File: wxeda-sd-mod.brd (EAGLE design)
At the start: 101.3 x 40.6 mm, 26 parts, among them T1 2N3904, U1 SD_CARD, X1 TV OUT, X2 TAPE IN / OUT

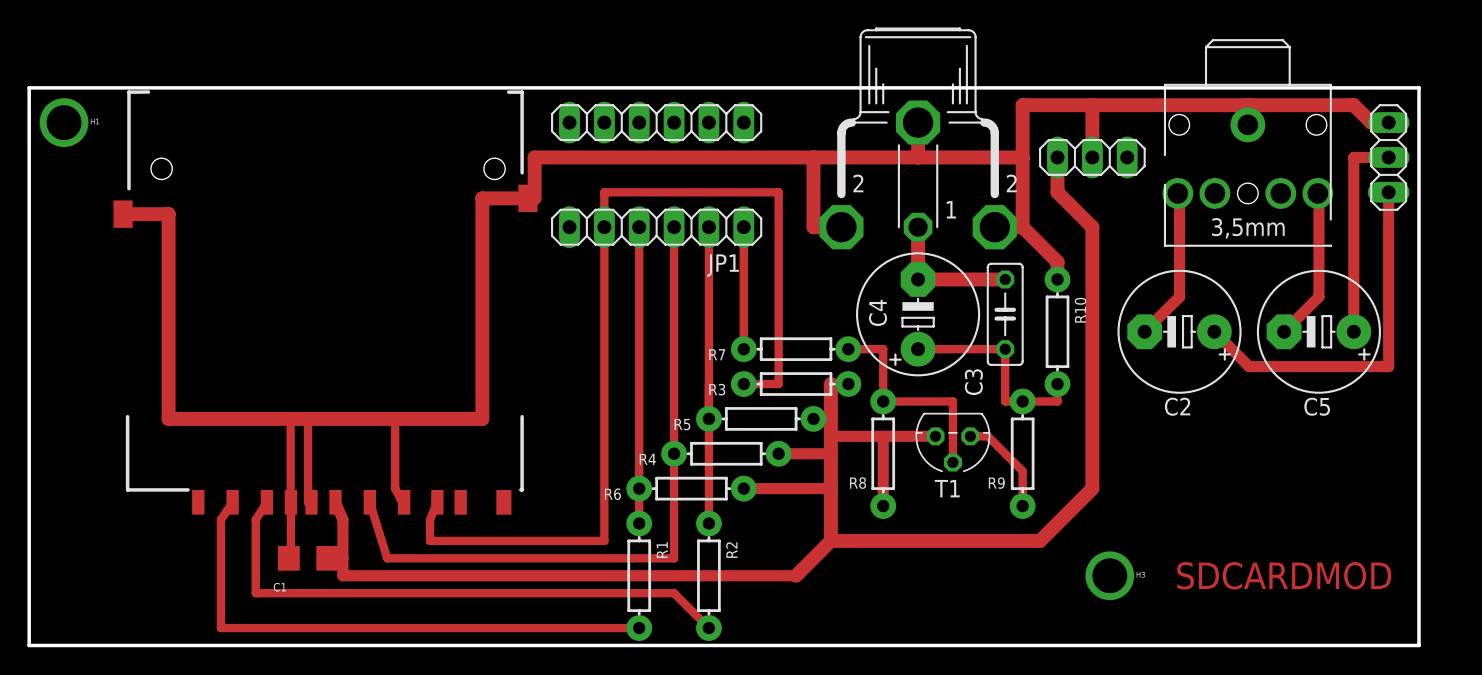
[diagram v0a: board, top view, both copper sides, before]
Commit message: Added stereo out
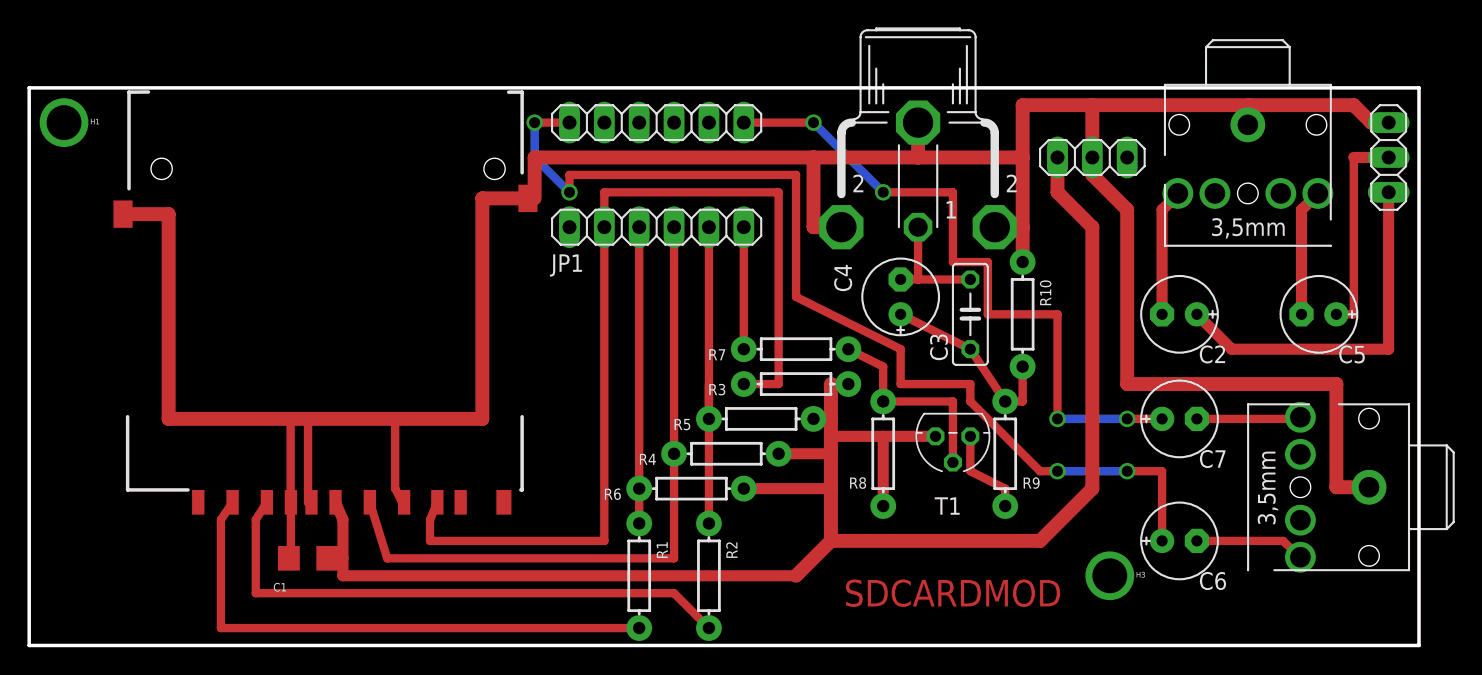
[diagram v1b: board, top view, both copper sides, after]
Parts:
- added C6, C7: 10uF, adafruit:E2,5-6E
- added X3: STEREO OUT, adafruit:STX3100
- C2, C4, C5: device adafruit:E5-8,5 -> adafruit:E2,5-6E
- moved R10 2.84 mm to (72.4, 24.1)
- moved C3 2.54 mm to (68.6, 24.1)
- moved C4 1.80 mm to (63.5, 25.4)
- moved C2 1.27 mm to (83.8, 24.1)
- moved C5 1.27 mm to (94.0, 24.1)
- moved R9 1.27 mm to (71.1, 14.0)
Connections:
- new net N$11: C7.-, X3.5
- new net N$9: C6.-, X3.2
- net DSB: now also C7.+
- net DSEN1: now also C6.+
- net GND: now also X3.1
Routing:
- net DSEN1: track 0.00 -> 73.9 mm, vias 0 -> 4
- net DSB: track 0.00 -> 49.1 mm, vias 0 -> 4
- net GND: track 180.9 -> 221.3 mm
- net N$9: track 0.00 -> 8.01 mm
- net N$11: track 0.00 -> 7.66 mm
- net N$4: track 11.3 -> 9.48 mm
- net N$6: track 11.2 -> 9.44 mm
- net TVOUT: track 10.2 -> 8.89 mm
- net N$8: track 15.2 -> 14.1 mm
- net N$2: track 15.9 -> 14.9 mm
- net N$7: track 7.40 -> 6.65 mm

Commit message: small improvements
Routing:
- net GND: track 221.3 -> 220.0 mm
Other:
- board text added: "RCA version"
- board text added: "STEREO OUT"
- board text added: "TAPE IN/OUT"
- board text added: "VIDEO OUT"
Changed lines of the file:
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@@
 <dimension x1="0" y1="0" x2="0" y2="40.64" x3="-7.62" y3="20.32" textsize="1.778" layer="20"/>
 <dimension x1="0" y1="40.63" x2="101.6" y2="40.64" x3="50.79925" y3="48.255" textsize="1.778" layer="20"/>
-<text x="67.31" y="3.81" size="1.9304" layer="1" rot="SR0" align="center">SDCARDMOD</text>
+<text x="67.31" y="5.08" size="1.9304" layer="1" rot="SR0" align="center">SDCARDMOD</text>
+<text x="67.31" y="2.54" size="1.9304" layer="1" rot="SR0" align="center">RCA version</text>
+<text x="88.9" y="3.81" size="1.27" layer="25">STEREO OUT</text>
+<text x="82.55" y="26.67" size="1.27" layer="25">TAPE IN/OUT</text>
+<text x="57.15" y="26.67" size="1.27" layer="25" rot="R90">VIDEO OUT</text>
 </plain>
 <attributes>
@@
 <element name="JP2" library="pinhead" package="1X03" value="IRDA" x="77.47" y="35.56" smashed="yes" rot="R180"/>
 <element name="U1" library="SparkFun-Connectors" package="SDCARD_4UCONN" value="SD_CARD" x="21.59" y="11.43" smashed="yes" rot="R90">
-<attribute name="VALUE" x="17.54" y="22.13" size="1.27" layer="27" ratio="10"/>
+<attribute name="VALUE" x="8.65" y="13.24" size="1.27" layer="27" ratio="10"/>
 </element>
 <element name="JP3" library="pinhead" package="1X06" value="7SEG_HR" x="45.72" y="38.1" smashed="yes"/>
@@
 <wire x1="36.34" y1="32.58" x2="36.83" y2="32.58" width="0.6096" layer="1"/>
 <wire x1="36.83" y1="32.58" x2="36.83" y2="35.56" width="1.016" layer="1"/>
-<wire x1="36.83" y1="35.56" x2="57.15" y2="35.56" width="1.016" layer="1"/>
-<wire x1="57.15" y1="35.56" x2="57.15" y2="30.48" width="1.016" layer="1"/>
+<wire x1="36.83" y1="35.56" x2="58.42" y2="35.56" width="1.016" layer="1"/>
+<wire x1="58.42" y1="35.56" x2="58.42" y2="30.48" width="1.016" layer="1"/>
 <wire x1="72.39" y1="35.56" x2="72.39" y2="39.37" width="1.016" layer="1"/>
 <wire x1="72.39" y1="39.37" x2="77.47" y2="39.37" width="1.016" layer="1"/>
@@
 <contactref element="X1" pad="2@2"/>
 <contactref element="X1" pad="2@1"/>
-<wire x1="59.182" y1="30.48" x2="57.15" y2="30.48" width="1.016" layer="1"/>
+<wire x1="59.182" y1="30.48" x2="58.42" y2="30.48" width="1.016" layer="1"/>
 <wire x1="70.358" y1="30.48" x2="72.39" y2="30.48" width="1.016" layer="1"/>
 <contactref element="X2" pad="1"/>
 <wire x1="72.39" y1="30.48" x2="72.39" y2="35.56" width="1.016" layer="1"/>
 <wire x1="72.39" y1="35.56" x2="64.77" y2="35.56" width="1.016" layer="1"/>
-<wire x1="64.77" y1="35.56" x2="57.15" y2="35.56" width="1.016" layer="1"/>
+<wire x1="64.77" y1="35.56" x2="58.42" y2="35.56" width="1.016" layer="1"/>
 <wire x1="64.77" y1="38.1" x2="64.77" y2="35.56" width="1.016" layer="1"/>
 <wire x1="72.39" y1="30.48" x2="72.39" y2="27.94" width="1.016" layer="1"/>
@@
 <via x="80.01" y="16.51" extent="1-16" drill="0.8" shape="square"/>
 <via x="74.93" y="16.51" extent="1-16" drill="0.8" shape="square"/>
-<wire x1="80.01" y1="16.51" x2="82.55" y2="16.51" width="0.6096" layer="1"/>
+<wire x1="80.01" y1="16.51" x2="82.55" y2="16.51" width="0.8128" layer="1"/>
 <wire x1="62.23" y1="33.02" x2="57.15" y2="38.1" width="0.6096" layer="16"/>
 <via x="57.15" y="38.1" extent="1-16" drill="0.8" shape="square"/>
@@
 <via x="74.93" y="12.7" extent="1-16" drill="0.8" shape="square"/>
 <via x="39.37" y="33.02" extent="1-16" drill="0.8" shape="square"/>
-<wire x1="82.55" y1="12.7" x2="82.55" y2="7.62" width="0.6096" layer="1"/>
-<wire x1="80.01" y1="12.7" x2="82.55" y2="12.7" width="0.6096" layer="1"/>
+<wire x1="82.55" y1="12.7" x2="82.55" y2="7.62" width="0.8128" layer="1"/>
+<wire x1="80.01" y1="12.7" x2="82.55" y2="12.7" width="0.8128" layer="1"/>
 <wire x1="36.83" y1="35.56" x2="36.83" y2="38.1" width="0.6096" layer="16"/>
 <wire x1="39.37" y1="33.02" x2="36.83" y2="35.56" width="0.6096" layer="16"/>
@@
 <contactref element="X3" pad="2"/>
 <contactref element="C6" pad="-"/>
-<wire x1="85.09" y1="7.62" x2="91.36" y2="7.62" width="0.6096" layer="1"/>
-<wire x1="91.36" y1="7.62" x2="92.63" y2="6.43" width="0.6096" layer="1"/>
+<wire x1="85.09" y1="7.62" x2="91.36" y2="7.62" width="0.8128" layer="1"/>
+<wire x1="91.36" y1="7.62" x2="92.63" y2="6.43" width="0.8128" layer="1"/>
 </signal>
 <signal name="N$11">
 <contactref element="X3" pad="5"/>
 <contactref element="C7" pad="-"/>
-<wire x1="85.09" y1="16.51" x2="92.63" y2="16.51" width="0.6096" layer="1"/>
+<wire x1="85.09" y1="16.51" x2="92.63" y2="16.51" width="0.8128" layer="1"/>
 <wire x1="92.63" y1="16.51" x2="92.63" y2="16.63" width="0.6096" layer="1"/>
 </signal>

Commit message: Added simplified version
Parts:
- removed C2, C5: 10uF, adafruit:E2,5-6E
- removed C3: 22n, adafruit:C050-025X075
- removed C4: 47uF, adafruit:E2,5-6E
- removed H3: SEW_HOLE, LilyPad-Wearables:SIMPLE_HOLE
- removed JP3: 7SEG_HR, pinhead:1X06
- removed JP4: ADC, pinhead:1X03
- removed R10: 150, SparkFun-Passives:AXIAL-0.3
- removed R9: 51, SparkFun-Passives:AXIAL-0.3
- removed T1: 2N3904, transistor:TO92
- removed X1: TV OUT, con-hirschmann:TOBU3
- removed X2: TAPE IN / OUT, adafruit:STX3100
- R7: value 680 -> 0
- R8: value 1k -> 0
- moved X3 44.2 mm to (66.0, 39.4), turned to 270 degrees
- moved C7 21.3 mm to (63.5, 22.9)
- moved C6 20.7 mm to (69.8, 22.9)
- moved R7 19.1 mm to (74.9, 22.9), turned to 90 degrees
- moved R8 13.1 mm to (55.9, 25.4), turned to 180 degrees
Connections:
- removed net A_IN: C5.+, JP4.2
- removed net DSA: JP3.2
- removed net DSB: C7.+, JP3.6
- removed net DSEN1: C6.+, JP3.1
- removed net DSEN2: JP3.4
- removed net DSEN3: JP3.5
- removed net DSF: JP3.3
- removed net GREEN: C2.+, JP4.3
- removed net N$6: C5.-, X2.2
- removed net N$7: R9.P$1, T1.3
- removed net N$8: C3.1, C4.+, R10.P$2, R9.P$2
- removed net TVOUT: C3.2, C4.-, X1.1
- net DSE: now also R7.P$2
- net DSEN4: now also R8.P$2; no longer R7.P$1
- net GND: no longer JP4.1, R10.P$1, X1.2, X1.2@1, X1.2@2, X2.1
- net N$2: now also C6.+, R7.P$1; no longer R7.P$2, R8.P$1, T1.2
- net N$4: now also C7.+, R8.P$1; no longer C2.-, X2.5
- net VCC: no longer R8.P$2, T1.1
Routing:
- net GND: track 220.0 -> 135.9 mm
- net DSEN1: track 73.9 -> 0.00 mm, vias 4 -> 0
- net DSB: track 49.1 -> 0.00 mm, vias 4 -> 0
- net DSE: track 0.00 -> 45.5 mm
- net GREEN: track 26.5 -> 0.00 mm
- net VCC: track 125.9 -> 107.8 mm
- net A_IN: track 15.2 -> 0.00 mm
- net N$8: track 14.1 -> 0.00 mm
- net N$6: track 9.44 -> 0.00 mm
- net TVOUT: track 8.89 -> 0.00 mm
- net N$7: track 6.65 -> 0.00 mm
- net N$4: track 9.48 -> 3.59 mm
- net N$2: track 14.9 -> 10.2 mm
- net DSEN4: track 8.89 -> 5.08 mm
- net N$11: track 7.66 -> 9.91 mm
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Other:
- board size 101.3 x 40.6 mm -> 82.2 x 40.6 mm
- board text added: "SD ONLY version"
- board text removed: "RCA version"
- board text removed: "TAPE IN/OUT"
- board text removed: "VIDEO OUT"
